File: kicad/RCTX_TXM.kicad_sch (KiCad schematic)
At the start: 18 parts

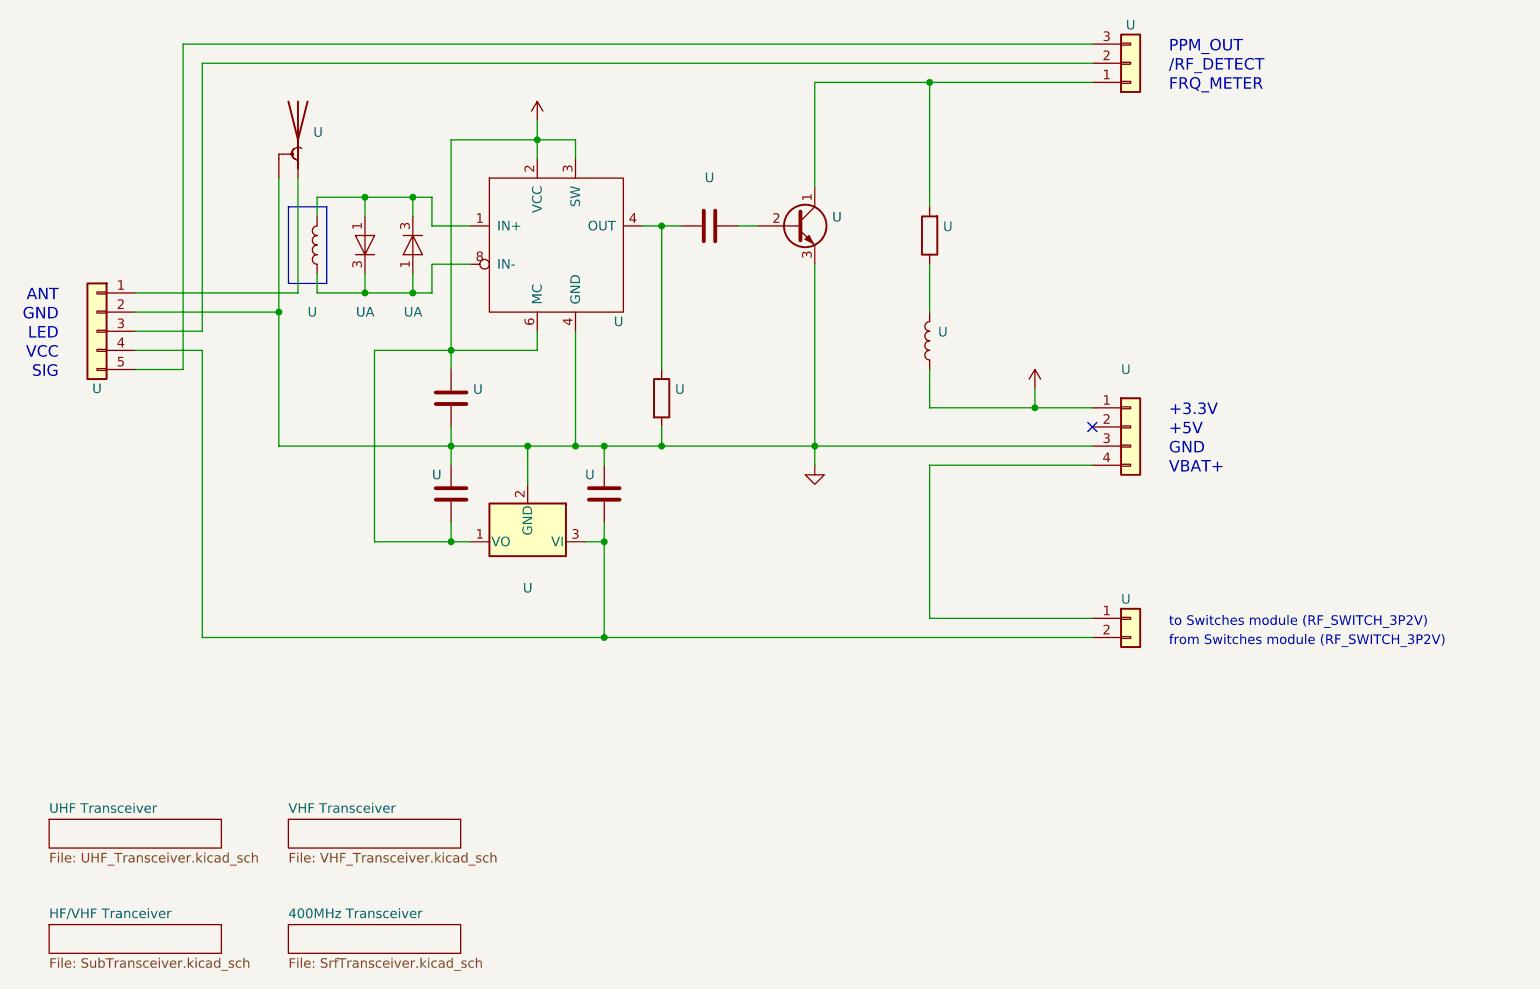
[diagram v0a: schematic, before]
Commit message: Adding PIB USB BRIDGE UML state diagrams - WIP
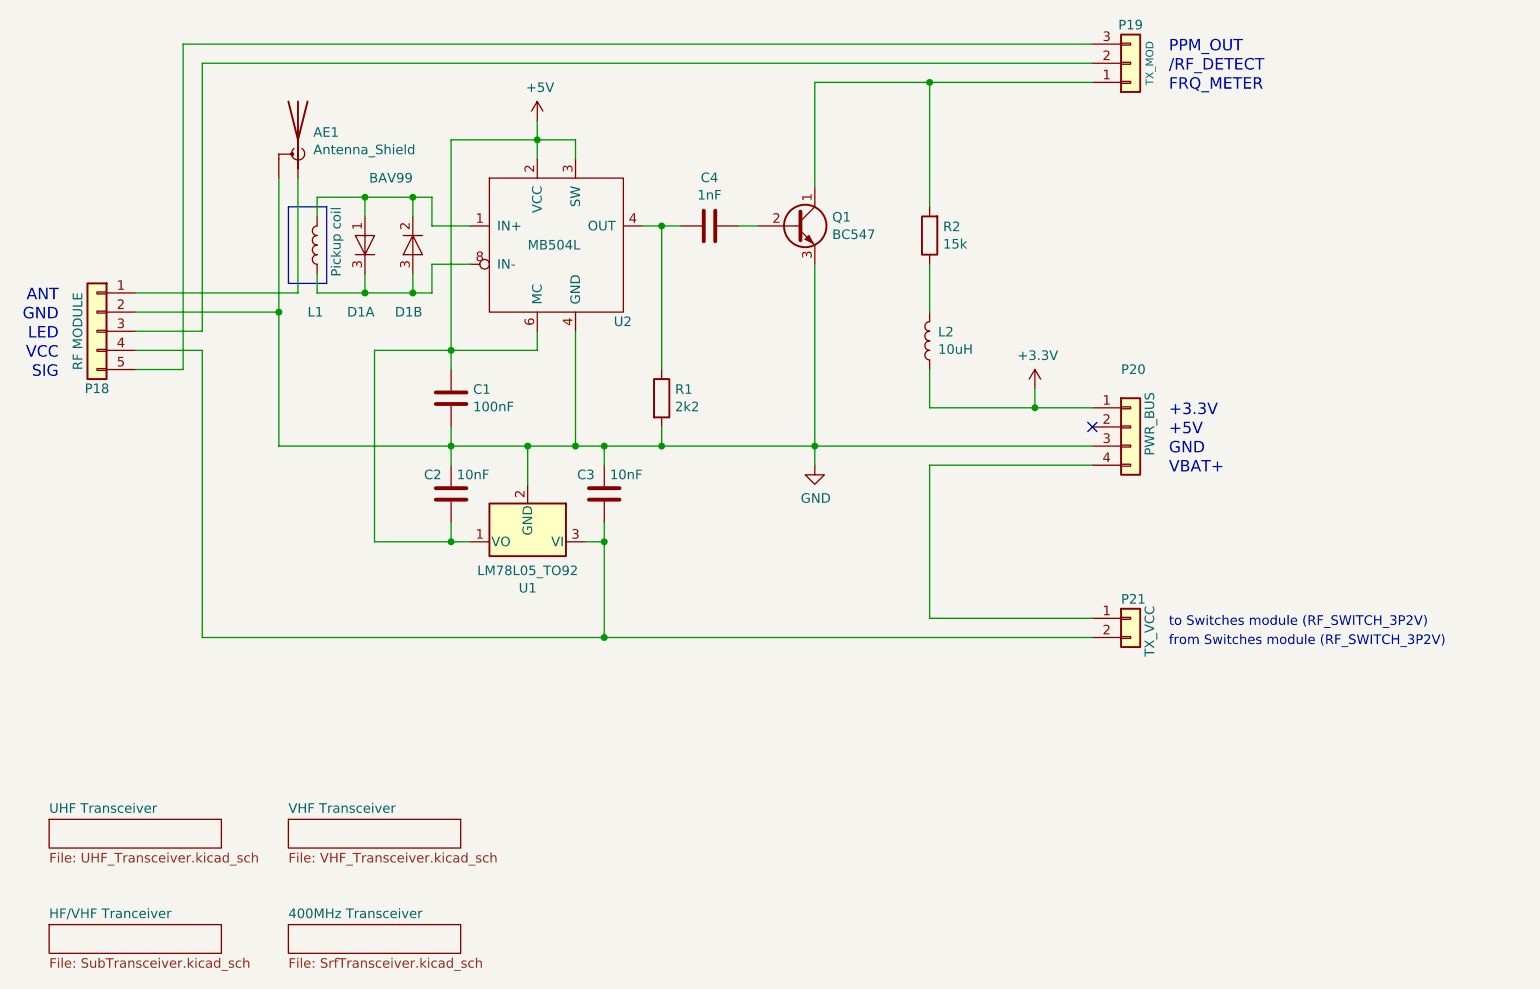
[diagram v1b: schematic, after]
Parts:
- AE1: renamed from U; value (none) -> Antenna_Shield; footprint (none) -> Connectors_Samtec:SL-102-X-XX_1x02
- C1: renamed from U; value (none) -> 100nF; footprint (none) -> Capacitors_THT:C_Disc_D3.0mm_W1.6mm_P2.50mm
- C2, C3: renamed from U; value (none) -> 10nF; footprint (none) -> Capacitors_THT:C_Disc_D3.0mm_W1.6mm_P2.50mm
- C4: renamed from U; value (none) -> 1nF; footprint (none) -> Capacitors_THT:C_Disc_D3.0mm_W1.6mm_P2.50mm
- D1: renamed from U; value (none) -> BAV99; footprint (none) -> TO_SOT_Packages_SMD:SOT-23
- L1: renamed from U; value (none) -> Pickup coil; footprint (none) -> Inductors_THT:L_Axial_L5.3mm_D2.2mm_P2.54mm_Vertical_Vishay_IM-1
- L2: renamed from U; value (none) -> 10uH; footprint (none) -> Inductors_THT:L_Axial_L5.3mm_D2.2mm_P2.54mm_Vertical_Vishay_IM-1
- P18: renamed from U; value (none) -> RF MODULE; footprint (none) -> Connectors_Samtec:SL-105-X-XX_1x05
- P19: renamed from U; value (none) -> TX_MOD; footprint (none) -> Connectors_Samtec:SL-103-X-XX_1x03
- P20: renamed from U; value (none) -> PWR_BUS; footprint (none) -> Connectors_Samtec:SL-104-X-XX_1x04
- P21: renamed from U; value (none) -> TX_VCC; footprint (none) -> Connectors_Samtec:SL-102-X-XX_1x02
- Q1: renamed from U; value (none) -> BC547; footprint (none) -> TO_SOT_Packages_THT:TO-92_Molded_Narrow
- R1: renamed from U; value (none) -> 2k2; footprint (none) -> Resistors_THT:R_Axial_DIN0204_L3.6mm_D1.6mm_P1.90mm_Vertical
- R2: renamed from U; value (none) -> 15k; footprint (none) -> Resistors_THT:R_Axial_DIN0204_L3.6mm_D1.6mm_P1.90mm_Vertical
- U1: renamed from U; value (none) -> LM78L05_TO92; footprint (none) -> TO_SOT_Packages_THT:TO-92_Inline_Narrow_Oval
- U2: renamed from U; value (none) -> MB504L; footprint (none) -> Housings_DIP:DIP-8_W7.62mm
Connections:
- net at D1.1 (A), L1.1, U2.1 (IN+): now also D1.2 (K); no longer D1.3 (K)
- net at D1.3 (K), L1.2, U2.8 (IN-): now also D1.3 (A); no longer D1.1 (A)
